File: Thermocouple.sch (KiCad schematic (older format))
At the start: 0 parts

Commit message: Completed -Defining IO Video
http://contextualelectronics.com/module-2/defining-your-inputs-and-outputs/
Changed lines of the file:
@@
 Comment4 ""
 $EndDescr
-Text HLabel 2000 2050 2    60   Input ~ 0
+Text HLabel 6550 2200 2    60   Input ~ 0
 TC IN +
-Text HLabel 2000 2350 2    60   Input ~ 0
+Text HLabel 6550 2500 2    60   Input ~ 0
 TC IN -
+Text HLabel 1600 1850 0    60   Input ~ 0
+MOSI
+Text HLabel 1600 2050 0    60   Output ~ 0
+MISO
+Text HLabel 1600 2250 0    60   Input ~ 0
+SCLK
+Text HLabel 1600 2450 0    60   Input ~ 0
+CS_N
 $EndSCHEMATC

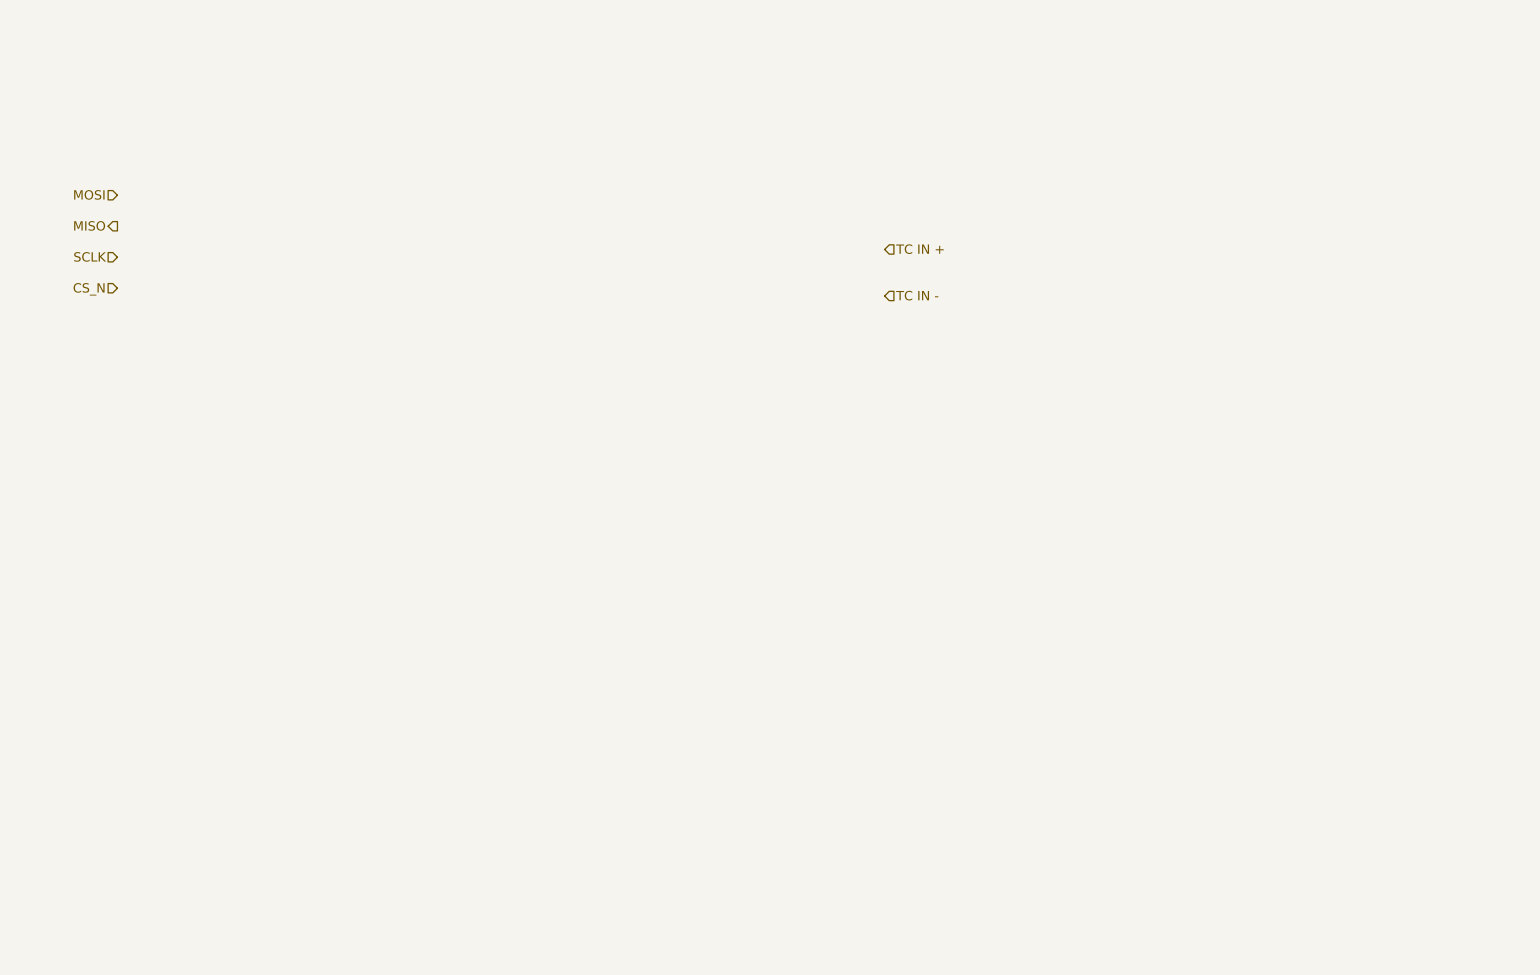
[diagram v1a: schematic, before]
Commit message: Started Thermocouple Schematic -Not Complete
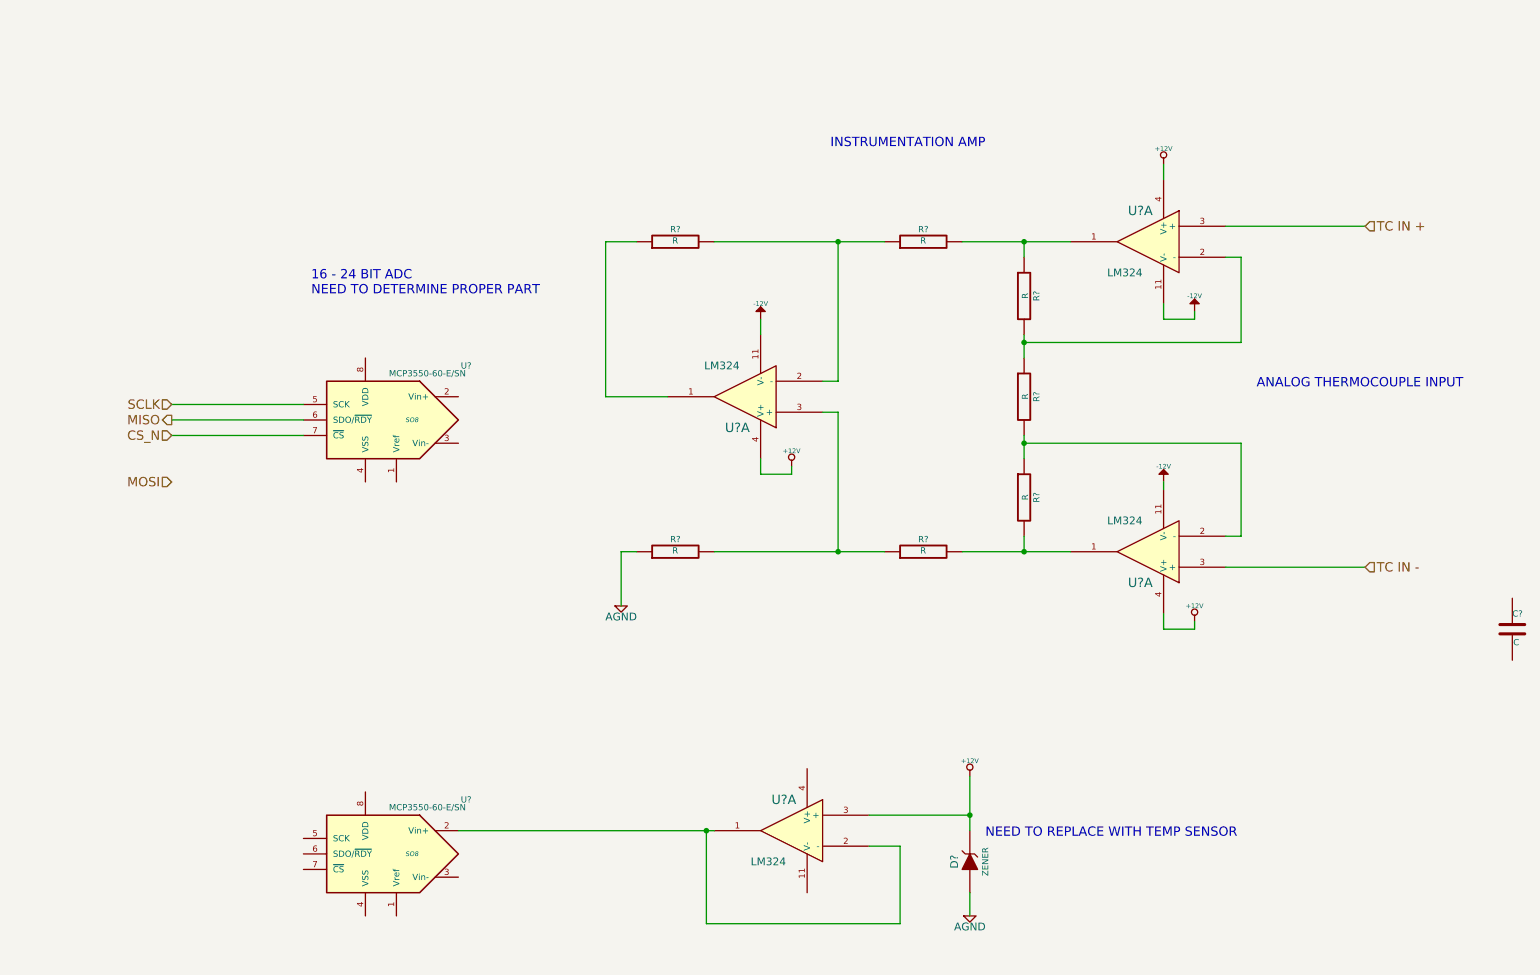
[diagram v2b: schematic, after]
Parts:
- added C?: C, ~, symbol C
- added D?: ZENER, ~, symbol ZENER
- added R? (x7): R, ~, symbol R
- added U? (x4): LM324, symbol LM324
- added U? (x2): MCP3550-60-E/SN, SO8, symbol MCP3550-60-E/SN
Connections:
- net CS_N: now also U?.7 (~CS~)
- net MISO: now also U?.6 (SDO/~RDY~)
- net SCLK: now also U?.5 (SCK)
- net TC IN +: now also U?.3 (+)
- net TC IN -: now also U?.3 (+)
- new net: R?.1, R?.2, U?.1
- new net: R?.1, R?.2, U?.2 (-) (x3)
- new net: R?.2, R?.2, U?.1
- new net: R?.1, U?.1
- new net: R?.1, R?.2, U?.3 (+)
- new net: U?.1, U?.2 (-), U?.2 (Vin+)
- new net +12V: D?.2 (K), U?.3 (+), U?.4 (V+), U?.4 (V+), U?.4 (V+)
- new net -12V: U?.11 (V-), U?.11 (V-), U?.11 (V-)
- new net AGND: D?.1 (A), R?.1
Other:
- note added: "16 - 24 BIT ADC\nNEED TO DETERMINE PROPER PART"
- note added: "ANALOG THERMOCOUPLE INPUT"
- note added: "INSTRUMENTATION AMP"
- note added: "NEED TO REPLACE WITH TEMP SENSOR"

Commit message: Started Layout Outline.  Completed other schem videos
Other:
- note added: "LMT86DCKT\nTEXAS INSTRUMENTS"
- note added: "MCP3901\nMICROCHIP"
- note added: "OPA4170AIDR\nTEXAS INSTRUMENTS"
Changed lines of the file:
@@
 Sheet 3 9
 Title ""
-Date "11 feb 2014"
+Date "17 feb 2014"
 Rev ""
 Comp ""
@@
 Text Notes 2850 2500 0    60   ~ 0
 16 - 24 BIT ADC\nNEED TO DETERMINE PROPER PART
+Text Notes 3150 4000 0    60   ~ 0
+MCP3901\nMICROCHIP
+Text Notes 6400 1700 0    60   ~ 0
+OPA4170AIDR\nTEXAS INSTRUMENTS
+Text Notes 7550 6100 0    60   ~ 0
+LMT86DCKT\nTEXAS INSTRUMENTS
 $EndSCHEMATC

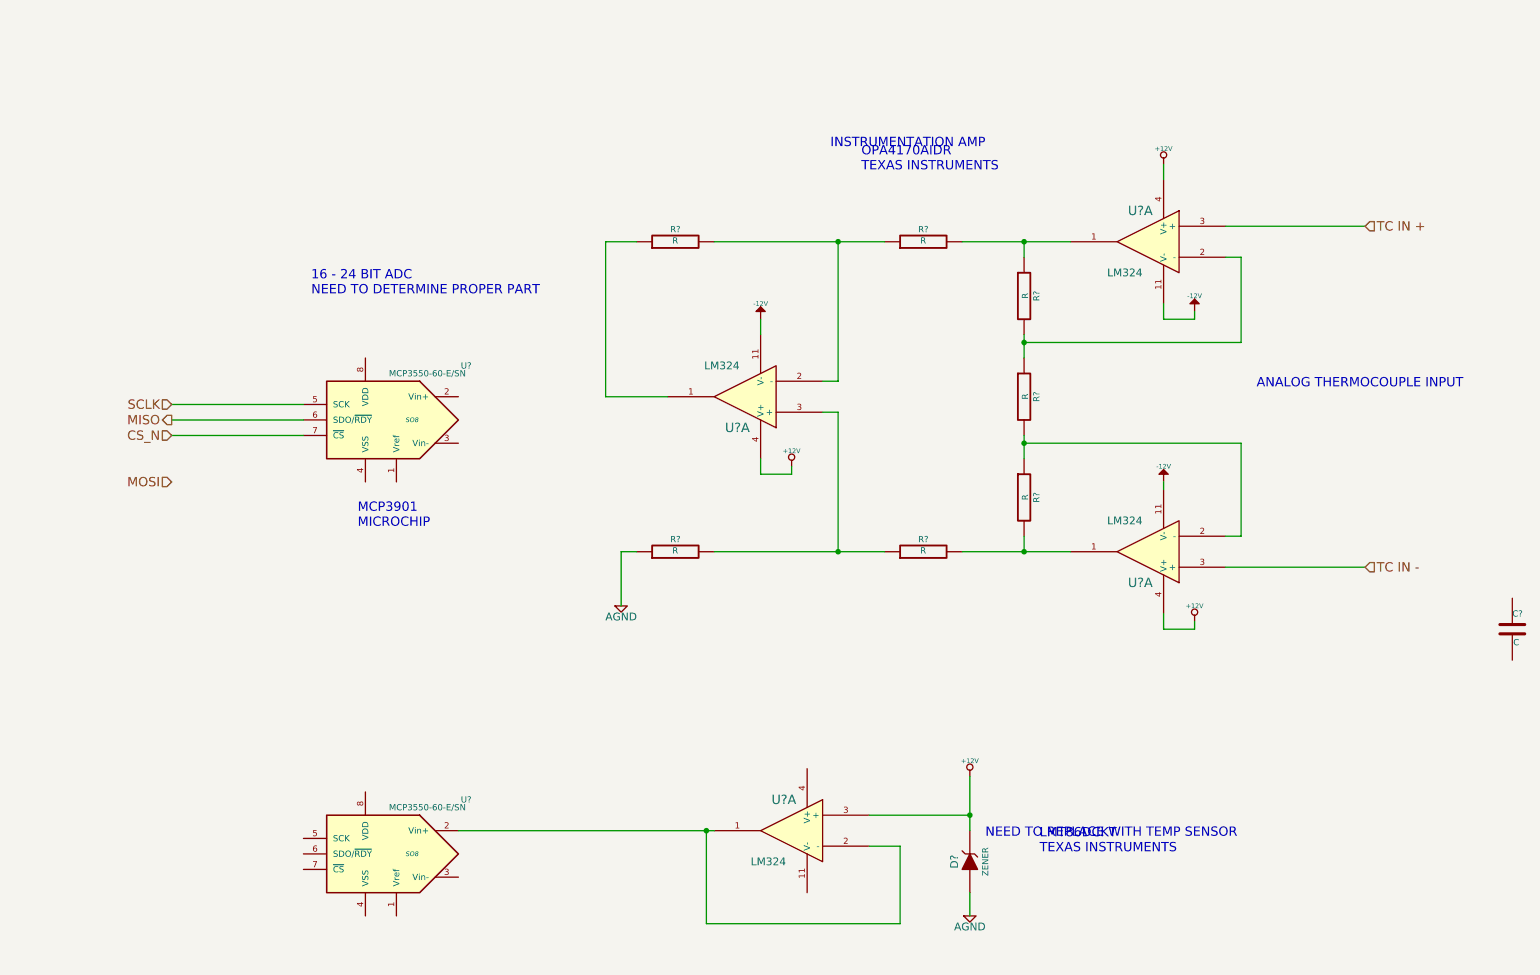
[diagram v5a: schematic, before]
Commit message: started associating relay parts
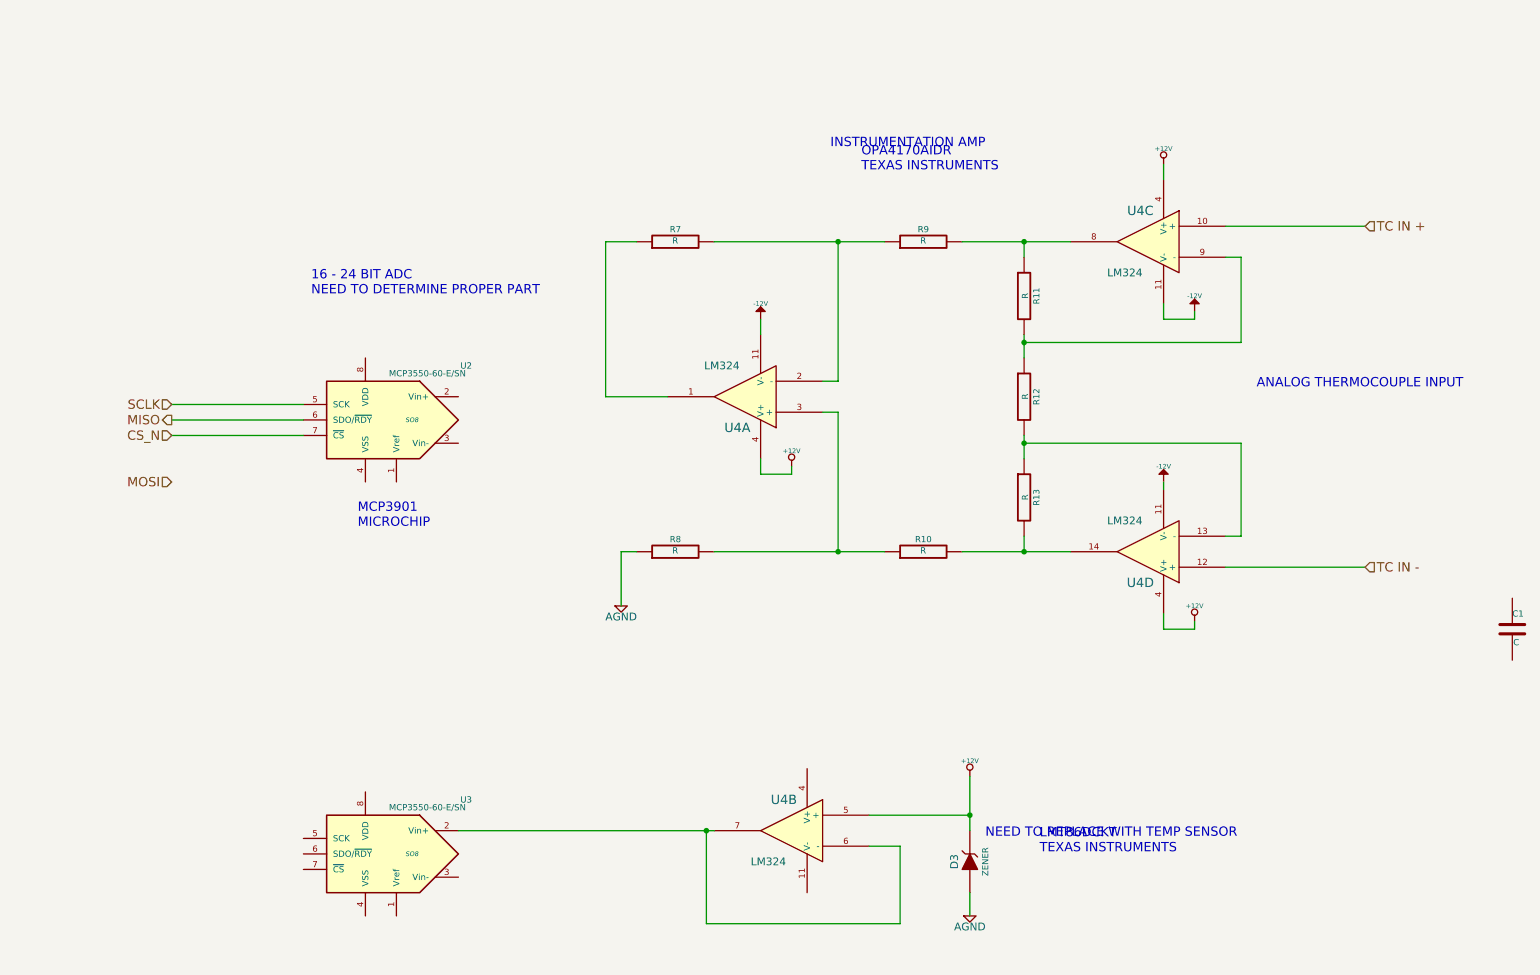
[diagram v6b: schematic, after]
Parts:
- gave numbers to parts that had none: 12
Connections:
- net +12V: now also U4.5 (+); no longer U4.3 (+)
- net TC IN +: now also U4.10 (+); no longer U4.3 (+)
- net TC IN -: now also U4.12 (+); no longer U4.3 (+)
- net at R11.1, R9.2: now also U4.8; no longer U4.1
- net at R11.2, R12.1: now also U4.9 (-); no longer U4.2 (-)
- net at R10.2, R13.2: now also U4.14; no longer U4.1
- net at R12.2, R13.1: now also U4.13 (-); no longer U4.2 (-)
- new net: U3.2 (Vin+), U4.6 (-), U4.7
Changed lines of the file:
@@
 Sheet 3 9
 Title ""
-Date "17 feb 2014"
+Date "20 feb 2014"
 Rev ""
 Comp ""
@@
 CS_N
 $Comp
-L LM324 U?
-U 1 1 52F2F542
+L LM324 U4
+U 3 1 52F2F542
 P 8250 2150
-F 0 "U?" H 8300 2350 60  0000 C CNN
+F 0 "U4" H 8300 2350 60  0000 C CNN
 F 1 "LM324" H 8400 1950 50  0000 C CNN
 F 2 "" H 8250 2150 60  0000 C CNN
 F 3 "" H 8250 2150 60  0000 C CNN
-	1    8250 2150
+	3    8250 2150
 	-1   0    0    -1
 $EndComp
 $Comp
-L LM324 U?
-U 1 1 52F2F54F
+L LM324 U4
+U 4 1 52F2F54F
 P 8250 4150
-F 0 "U?" H 8300 4350 60  0000 C CNN
+F 0 "U4" H 8300 4350 60  0000 C CNN
 F 1 "LM324" H 8400 3950 50  0000 C CNN
 F 2 "" H 8250 4150 60  0000 C CNN
 F 3 "" H 8250 4150 60  0000 C CNN
-	1    8250 4150
+	4    8250 4150
 	-1   0    0    1
 $EndComp
 $Comp
-L LM324 U?
+L LM324 U4
 U 1 1 52F2F555
 P 5650 3150
-F 0 "U?" H 5700 3350 60  0000 C CNN
+F 0 "U4" H 5700 3350 60  0000 C CNN
 F 1 "LM324" H 5800 2950 50  0000 C CNN
 F 2 "" H 5650 3150 60  0000 C CNN
@@
 $EndComp
 $Comp
-L LM324 U?
-U 1 1 52F2F55B
+L LM324 U4
+U 2 1 52F2F55B
 P 5950 5950
-F 0 "U?" H 6000 6150 60  0000 C CNN
+F 0 "U4" H 6000 6150 60  0000 C CNN
 F 1 "LM324" H 6100 5750 50  0000 C CNN
 F 2 "" H 5950 5950 60  0000 C CNN
 F 3 "" H 5950 5950 60  0000 C CNN
-	1    5950 5950
+	2    5950 5950
 	-1   0    0    -1
 $EndComp
 $Comp
-L R R?
+L R R12
 U 1 1 52F2F5A8
 P 7450 3150
-F 0 "R?" V 7530 3150 40  0000 C CNN
+F 0 "R12" V 7530 3150 40  0000 C CNN
 F 1 "R" V 7457 3151 40  0000 C CNN
 F 2 "~" V 7380 3150 30  0000 C CNN
@@
 $EndComp
 $Comp
-L C C?
+L C C1
 U 1 1 52F2F5B7
 P 10600 4650
-F 0 "C?" H 10600 4750 40  0000 L CNN
+F 0 "C1" H 10600 4750 40  0000 L CNN
 F 1 "C" H 10606 4565 40  0000 L CNN
 F 2 "~" H 10638 4500 30  0000 C CNN
@@
 $EndComp
 $Comp
-L R R?
+L R R11
 U 1 1 52F2F5D8
 P 7450 2500
-F 0 "R?" V 7530 2500 40  0000 C CNN
+F 0 "R11" V 7530 2500 40  0000 C CNN
 F 1 "R" V 7457 2501 40  0000 C CNN
 F 2 "~" V 7380 2500 30  0000 C CNN
@@
 $EndComp
 $Comp
-L R R?
+L R R13
 U 1 1 52F2F5DE
 P 7450 3800
-F 0 "R?" V 7530 3800 40  0000 C CNN
+F 0 "R13" V 7530 3800 40  0000 C CNN
 F 1 "R" V 7457 3801 40  0000 C CNN
 F 2 "~" V 7380 3800 30  0000 C CNN
@@
 	7050 4150 7750 4150
 $Comp
-L R R?
+L R R10
 U 1 1 52F2F5F1
 P 6800 4150
-F 0 "R?" V 6880 4150 40  0000 C CNN
+F 0 "R10" V 6880 4150 40  0000 C CNN
 F 1 "R" V 6807 4151 40  0000 C CNN
 F 2 "~" V 6730 4150 30  0000 C CNN
@@
 $EndComp
 $Comp
-L R R?
+L R R8
 U 1 1 52F2F625
 P 5200 4150
-F 0 "R?" V 5280 4150 40  0000 C CNN
+F 0 "R8" V 5280 4150 40  0000 C CNN
 F 1 "R" V 5207 4151 40  0000 C CNN
 F 2 "~" V 5130 4150 30  0000 C CNN
@@
 $EndComp
 $Comp
-L R R?
+L R R7
 U 1 1 52F2F62B
 P 5200 2150
-F 0 "R?" V 5280 2150 40  0000 C CNN
+F 0 "R7" V 5280 2150 40  0000 C CNN
 F 1 "R" V 5207 2151 40  0000 C CNN
 F 2 "~" V 5130 2150 30  0000 C CNN
@@
 $EndComp
 $Comp
-L R R?
+L R R9
 U 1 1 52F2F638
 P 6800 2150
-F 0 "R?" V 6880 2150 40  0000 C CNN
+F 0 "R9" V 6880 2150 40  0000 C CNN
 F 1 "R" V 6807 2151 40  0000 C CNN
 F 2 "~" V 6730 2150 30  0000 C CNN
@@
 	4750 3150 4750 2150
 $Comp
-L -12V #PWR?
+L -12V #PWR01
 U 1 1 52F2F9BF
 P 5750 2650
-F 0 "#PWR?" H 5750 2780 20  0001 C CNN
+F 0 "#PWR01" H 5750 2780 20  0001 C CNN
 F 1 "-12V" H 5750 2750 30  0000 C CNN
 F 2 "" H 5750 2650 60  0000 C CNN
@@
 $EndComp
 $Comp
-L -12V #PWR?
+L -12V #PWR02
 U 1 1 52F2F9CC
 P 8550 2600
-F 0 "#PWR?" H 8550 2730 20  0001 C CNN
+F 0 "#PWR02" H 8550 2730 20  0001 C CNN
 F 1 "-12V" H 8550 2700 30  0000 C CNN
 F 2 "" H 8550 2600 60  0000 C CNN
@@
 $EndComp
 $Comp
-L -12V #PWR?
+L -12V #PWR03
 U 1 1 52F2F9D3
 P 8350 3700
-F 0 "#PWR?" H 8350 3830 20  0001 C CNN
+F 0 "#PWR03" H 8350 3830 20  0001 C CNN
 F 1 "-12V" H 8350 3800 30  0000 C CNN
 F 2 "" H 8350 3700 60  0000 C CNN
@@
 	5750 2750 5750 2650
 $Comp
-L +12V #PWR?
+L +12V #PWR04
 U 1 1 52F2FA49
 P 5950 3600
-F 0 "#PWR?" H 5950 3550 20  0001 C CNN
+F 0 "#PWR04" H 5950 3550 20  0001 C CNN
 F 1 "+12V" H 5950 3700 30  0000 C CNN
 F 2 "" H 5950 3600 60  0000 C CNN
@@
 	8550 2650 8550 2600
 $Comp
-L +12V #PWR?
+L +12V #PWR05
 U 1 1 52F2FAEF
 P 8350 1650
-F 0 "#PWR?" H 8350 1600 20  0001 C CNN
+F 0 "#PWR05" H 8350 1600 20  0001 C CNN
 F 1 "+12V" H 8350 1750 30  0000 C CNN
 F 2 "" H 8350 1650 60  0000 C CNN
@@
 $EndComp
 $Comp
-L +12V #PWR?
+L +12V #PWR06
 U 1 1 52F2FAF5
 P 8550 4600
-F 0 "#PWR?" H 8550 4550 20  0001 C CNN
+F 0 "#PWR06" H 8550 4550 20  0001 C CNN
 F 1 "+12V" H 8550 4700 30  0000 C CNN
 F 2 "" H 8550 4600 60  0000 C CNN
@@
 	8350 4650 8350 4550
 $Comp
-L AGND #PWR?
+L AGND #PWR07
 U 1 1 52F2FB5B
 P 4850 4500
-F 0 "#PWR?" H 4850 4500 40  0001 C CNN
+F 0 "#PWR07" H 4850 4500 40  0001 C CNN
 F 1 "AGND" H 4850 4430 50  0000 C CNN
 F 2 "" H 4850 4500 60  0000 C CNN
@@
 	4850 4150 4950 4150
 $Comp
-L MCP3550-60-E/SN U?
+L MCP3550-60-E/SN U2
 U 1 1 52F2FC1A
 P 3300 3300
-F 0 "U?" H 2750 3650 40  0000 C CNN
+F 0 "U2" H 2750 3650 40  0000 C CNN
 F 1 "MCP3550-60-E/SN" H 3000 3600 40  0000 C CNN
 F 2 "SO8" H 3100 3300 30  0000 C CIN
@@
 	1950 3200 2800 3200
 $Comp
-L MCP3550-60-E/SN U?
+L MCP3550-60-E/SN U3
 U 1 1 52F2FDB2
 P 3300 6100
-F 0 "U?" H 2750 6450 40  0000 C CNN
+F 0 "U3" H 2750 6450 40  0000 C CNN
 F 1 "MCP3550-60-E/SN" H 3000 6400 40  0000 C CNN
 F 2 "SO8" H 3100 6100 30  0000 C CIN
@@
 $EndComp
 $Comp
-L ZENER D?
+L ZENER D3
 U 1 1 52F2FDD8
 P 7100 6150
-F 0 "D?" H 7100 6250 50  0000 C CNN
+F 0 "D3" H 7100 6250 50  0000 C CNN
 F 1 "ZENER" H 7100 6050 40  0000 C CNN
 F 2 "~" H 7100 6150 60  0000 C CNN
@@
 	7100 5600 7100 5950
 $Comp
-L AGND #PWR?
+L AGND #PWR08
 U 1 1 52F2FE66
 P 7100 6500
-F 0 "#PWR?" H 7100 6500 40  0001 C CNN
+F 0 "#PWR08" H 7100 6500 40  0001 C CNN
 F 1 "AGND" H 7100 6430 50  0000 C CNN
 F 2 "" H 7100 6500 60  0000 C CNN
@@
 	7100 6350 7100 6500
 $Comp
-L +12V #PWR?
+L +12V #PWR09
 U 1 1 52F2FEA2
 P 7100 5600
-F 0 "#PWR?" H 7100 5550 20  0001 C CNN
+F 0 "#PWR09" H 7100 5550 20  0001 C CNN
 F 1 "+12V" H 7100 5700 30  0000 C CNN
 F 2 "" H 7100 5600 60  0000 C CNN
